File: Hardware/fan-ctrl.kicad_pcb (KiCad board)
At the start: 2 copper layers, 53 parts, among them CN1 DB127S-3.5-4P-GN, Q1 AO3401A, Q2 AO3400A, U1 STM32G070RBT6, U2 826629-3, U3 826629-3, U4 MP2359DT-LF-Z, U5 XDJK-0051-025, U6 AMS1117-3.3, Y1 Crystal_GND24

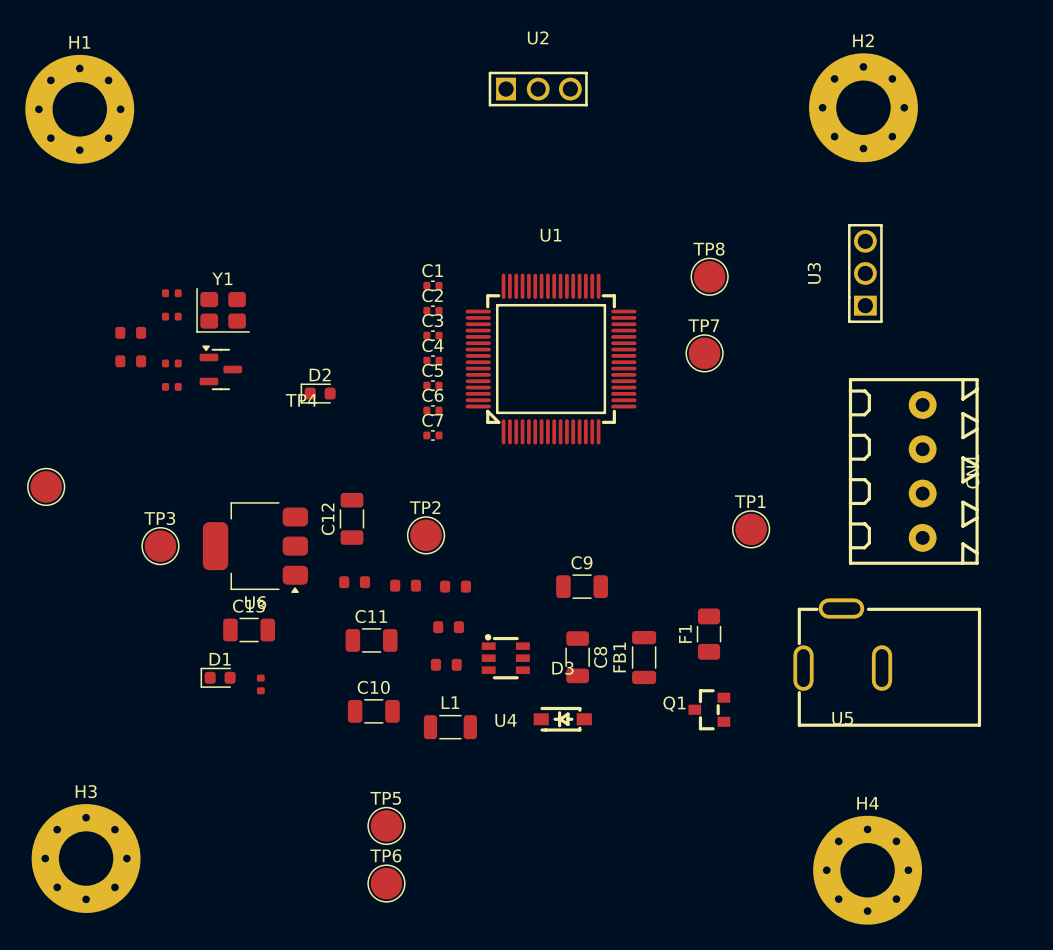
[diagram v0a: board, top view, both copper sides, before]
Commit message: Component placement, board edge cuts, adjust some footprints, testpoints, silkscreen for connectors and testpoints, next: review footprints JLCPCB before routing
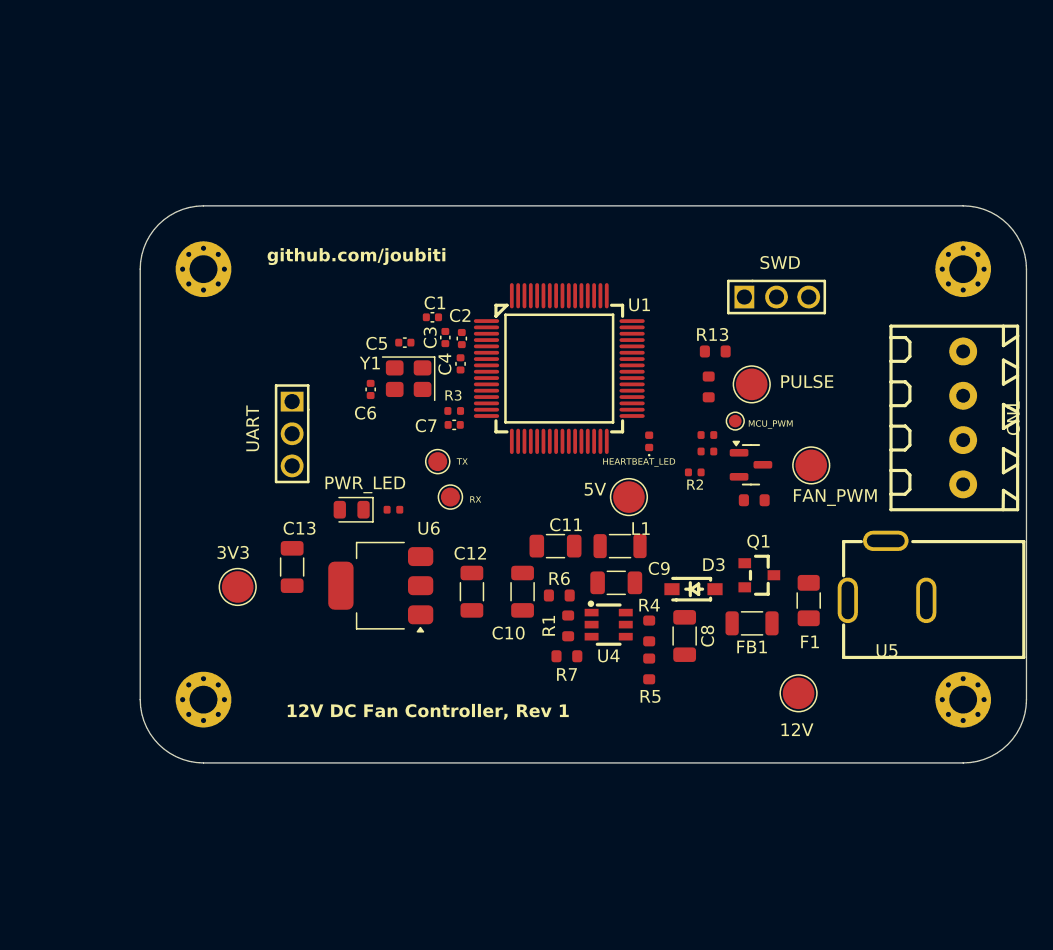
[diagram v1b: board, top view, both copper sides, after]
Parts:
- added R13: 10k, PCM_JLCPCB:R_0603, F.Cu at (163.4, 69.5)
- D1: footprint LED_SMD:LED_0603_1608Metric -> LED_SMD:LED_0805_2012Metric
- D2: footprint LED_SMD:LED_0603_1608Metric -> LED_SMD:LED_0402_1005Metric
- H1, H2, H3, H4: footprint MountingHole:MountingHole_4.3mm_M4_Pad_Via -> MountingHole:MountingHole_2.2mm_M2_Pad_Via
- TP4: footprint TestPoint:TestPoint_Pad_D2.5mm -> TestPoint:TestPoint_Pad_D1.0mm
- TP7, TP8: footprint TestPoint:TestPoint_Pad_D2.5mm -> TestPoint:TestPoint_Pad_D1.5mm
- moved TP4 54.7 mm to (165.0, 75.0)
- moved R10 50.5 mm to (166.5, 81.2)
- moved TP6 48.9 mm to (166.3, 72.1)
- moved U3 47.0 mm to (130.0, 76.0), turned to -90 degrees
- moved R9 45.8 mm to (162.9, 72.3), turned to -90 degrees
- moved TP5 44.0 mm to (171.0, 78.5)
- moved R2 43.7 mm to (161.8, 79.0)
- moved R11 42.7 mm to (162.8, 76.1)
- moved R12 42.6 mm to (162.8, 77.4)
- moved Q2 42.5 mm to (166.2, 78.5)
- moved TP8 26.9 mm to (142.5, 81.0)
- moved D2 26.3 mm to (158.2, 76.6), turned to 90 degrees
- moved U2 25.0 mm to (168.3, 65.2)
- moved R3 23.5 mm to (142.8, 74.2)
- moved TP7 22.7 mm to (141.5, 78.2)
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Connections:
- CN1 pad 1: +12V -> FAN_PULSE_IN
- CN1 pad 2: VSS -> FAN_PWM_INPUT
- CN1 pad 3: FAN_PULSE_IN -> VSS
- CN1 pad 4: FAN_PWM_INPUT -> +12V
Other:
- board outline added: 70 x 44 mm
- board text added: "12V"
- board text added: "12V DC Fan Controller, Rev 1"
- board text added: "3V3"
- board text added: "5V"
- board text added: "FAN_PWM"
- board text added: "HEARTBEAT_LED"
- board text added: "MCU_PWM"
- board text added: "PULSE"
- board text added: "PWR_LED"
- board text added: "RX"
- board text added: "SWD"
- board text added: "TX"
- board text added: "UART"
- board text added: "github.com/joubiti"

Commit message: Adjust board dimensions and edge cuts
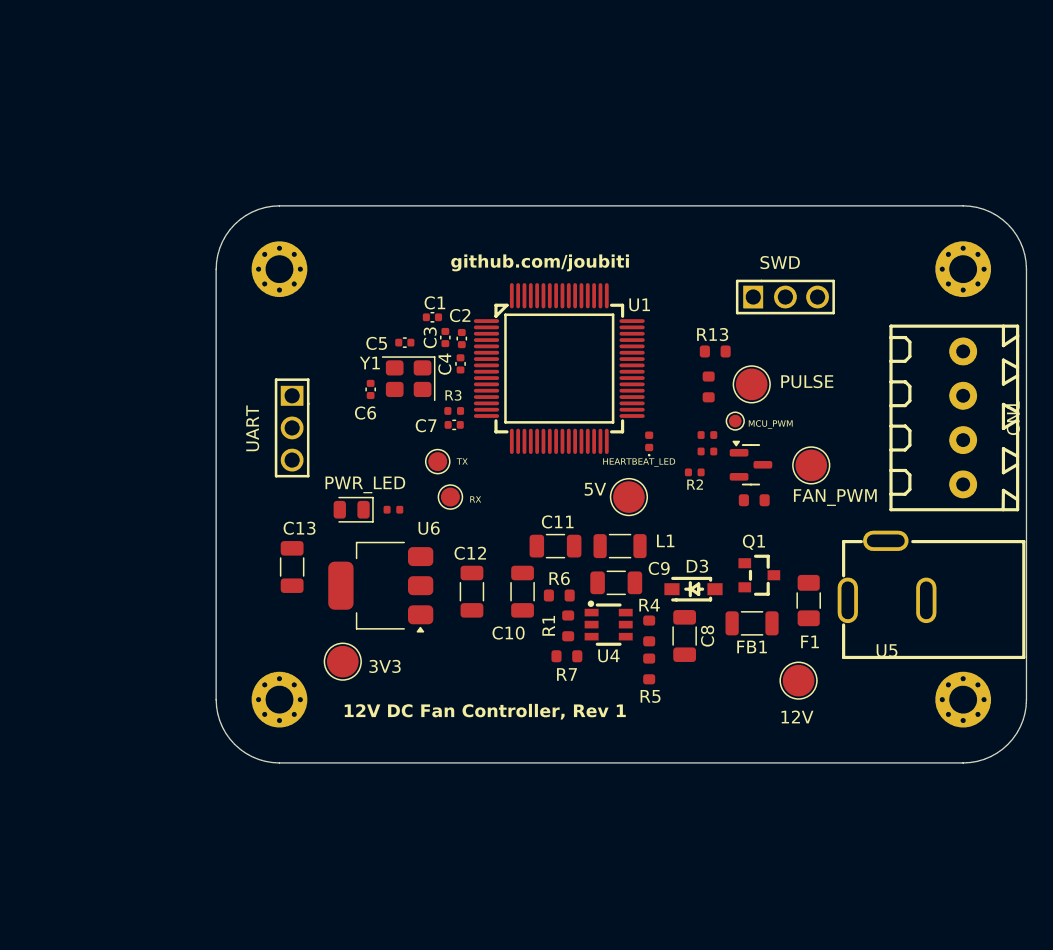
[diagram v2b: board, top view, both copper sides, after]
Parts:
- moved TP3 10.2 mm to (134.0, 94.0)
- moved H1 6.00 mm to (129.0, 63.0)
- moved H3 6.00 mm to (129.0, 97.0)
- moved TP1 1.00 mm to (170.0, 95.5)
- moved U2 0.70 mm to (169.0, 65.2)
- moved U3 0.46 mm to (130.0, 75.5)
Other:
- board size 70 x 44 mm -> 64 x 44 mm
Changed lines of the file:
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@@
 	(footprint "TestPoint:TestPoint_Pad_D2.5mm"
 		(layer "F.Cu")
-		(at 170 96.5)
+		(at 170 95.5)
 		(descr "SMD pad as test Point, diameter 2.5mm")
 		(tags "test point SMD pad")
@@
 		(at 166.9 87.175 180)
 		(property "Reference" "Q1"
-			(at 0.05 2.65 0)
+			(at 0.4 2.65 0)
 			(layer "F.SilkS")
 			(effects
@@
 	(footprint "MountingHole:MountingHole_2.2mm_M2_Pad_Via"
 		(layer "F.Cu")
-		(at 123 97)
+		(at 129 97)
 		(descr "Mounting Hole 2.2mm, M2, generated by kicad-footprint-generator mountinghole.py")
 		(tags "mountinghole M2")
@@
 		(at 161.7 88.275)
 		(property "Reference" "D3"
-			(at 1.6 -1.9 0)
+			(at 0.3 -1.775 0)
 			(layer "F.SilkS")
 			(effects
@@
 	(footprint "TestPoint:TestPoint_Pad_D2.5mm"
 		(layer "F.Cu")
-		(at 125.7 88.1)
+		(at 134 94)
 		(descr "SMD pad as test Point, diameter 2.5mm")
 		(tags "test point SMD pad")
@@
 	(footprint "MountingHole:MountingHole_2.2mm_M2_Pad_Via"
 		(layer "F.Cu")
-		(at 123 63)
+		(at 129 63)
 		(descr "Mounting Hole 2.2mm, M2, generated by kicad-footprint-generator mountinghole.py")
 		(tags "mountinghole M2")
@@
 		(tags "inductor")
 		(property "Reference" "L1"
-			(at -1.65 1.35 0)
+			(at -3.6 0.375 0)
 			(layer "F.SilkS")
 			(effects
@@
 	(footprint "easyeda2kicad:HDR-TH_3P-P2.54-V-M-1"
 		(layer "F.Cu")
-		(at 168.26 65.2)
+		(at 168.96 65.2)
 		(property "Reference" "U2"
 			(at 0 -2.5 0)
@@
 		(tags "capacitor")
 		(property "Reference" "C11"
-			(at -0.85 1.65 0)
+			(at -0.2 1.875 0)
 			(layer "F.SilkS")
 			(effects
@@
 	(footprint "easyeda2kicad:HDR-TH_3P-P2.54-V-M-1"
 		(layer "F.Cu")
-		(at 130 76 -90)
+		(at 130 75.54 -90)
 		(property "Reference" "U3"
 			(at -0.14 -2.6 90)
@@
 		)
 	)
-	(gr_arc
-		(start 183 58)
-		(mid 186.535534 59.464466)
-		(end 188 63)
+	(gr_line
+		(start 124 63)
+		(end 124 97)
 		(stroke
 			(width 0.05)
@@
 	)
 	(gr_arc
-		(start 118 63)
-		(mid 119.464466 59.464466)
-		(end 123 58)
+		(start 183 58)
+		(mid 186.535534 59.464466)
+		(end 188 63)
 		(stroke
 			(width 0.05)
@@
 		(layer "Edge.Cuts")
 	)
-	(gr_line
-		(start 123 58)
-		(end 183 58)
+	(gr_arc
+		(start 188 97)
+		(mid 186.535534 100.535534)
+		(end 183 102)
 		(stroke
 			(width 0.05)
@@
 	)
 	(gr_line
-		(start 123 102)
+		(start 129 102)
 		(end 183 102)
 		(stroke
@@
 	)
 	(gr_arc
-		(start 188 97)
-		(mid 186.535534 100.535534)
-		(end 183 102)
+		(start 124 63)
+		(mid 125.464466 59.464466)
+		(end 129 58)
 		(stroke
 			(width 0.05)
@@
 	)
 	(gr_arc
-		(start 123 102)
-		(mid 119.464466 100.535534)
-		(end 118 97)
+		(start 129 102)
+		(mid 125.464466 100.535534)
+		(end 124 97)
 		(stroke
 			(width 0.05)
@@
 	)
 	(gr_line
-		(start 118 97)
-		(end 118 63)
+		(start 129 58)
+		(end 183 58)
 		(stroke
 			(width 0.05)
@@
 	)
 	(gr_text "3V3"
-		(at 124 86 0)
+		(at 136 95 0)
 		(layer "F.SilkS")
 		(effects
@@
 	)
 	(gr_text "github.com/joubiti"
-		(at 128 62.5 0)
+		(at 142.5 63 0)
 		(layer "F.SilkS")
 		(effects
@@
 	)
 	(gr_text "12V DC Fan Controller, Rev 1"
-		(at 129.5 98.5 0)
+		(at 134 98.5 0)
 		(layer "F.SilkS")
 		(effects
@@
 	)
 	(gr_text "12V"
-		(at 168.5 100 0)
+		(at 168.5 99 0)
 		(layer "F.SilkS")
 		(effects

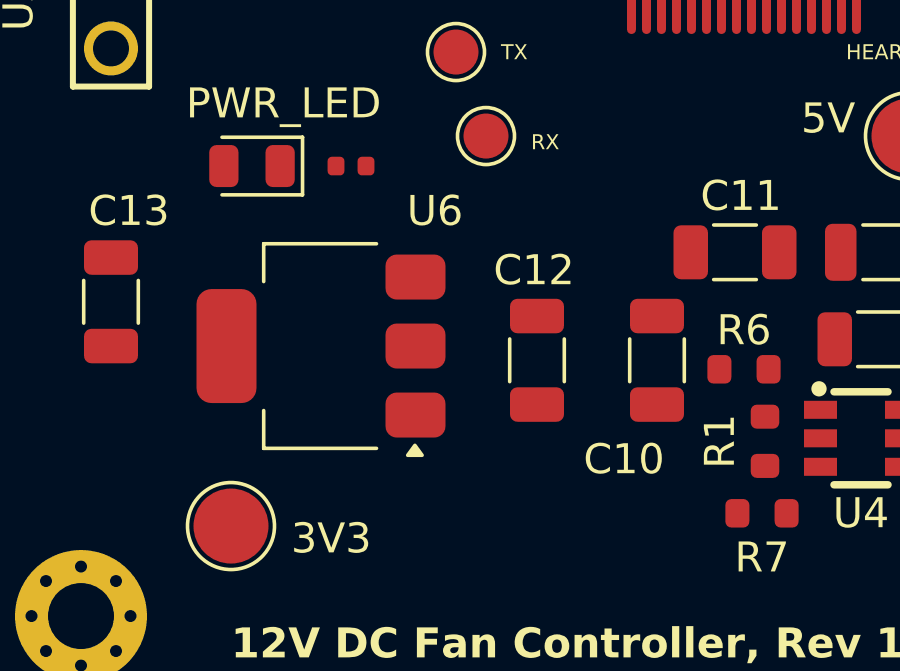
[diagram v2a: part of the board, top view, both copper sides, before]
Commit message: Update buck converter circuit, standard R values for close 5V output, double-checked footprints available in JLCPCB
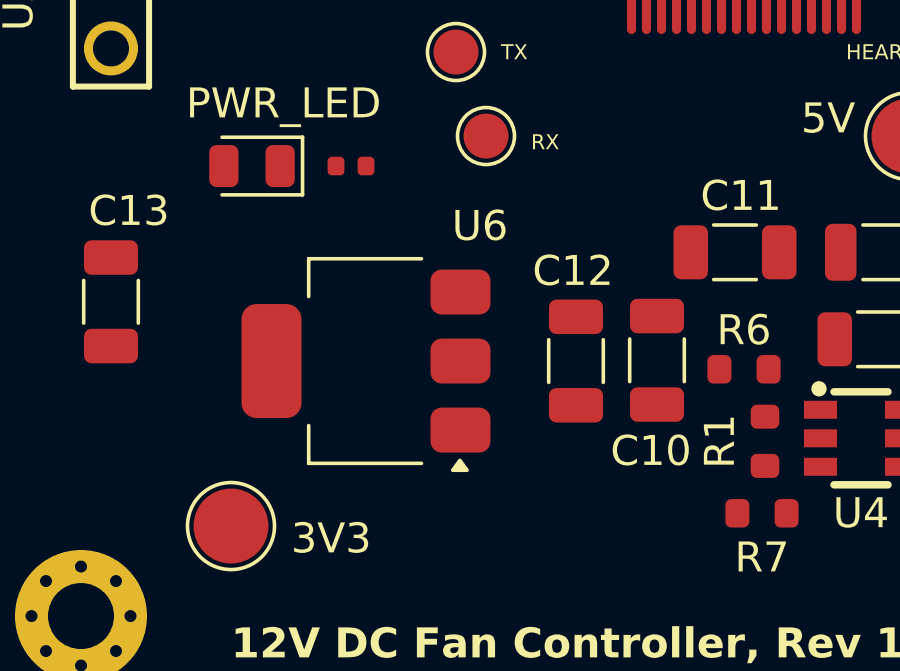
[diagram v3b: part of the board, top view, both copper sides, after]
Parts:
- L1: value 10u -> 4.7u
- R1: value 3k -> 49k9
- R7: value 10k -> 9k1
- moved U6 1.58 mm to (138.5, 88.5)
- moved C12 1.30 mm to (145.5, 88.5)
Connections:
- R1 pad 1: Net-(R1-Pad1) -> +5V
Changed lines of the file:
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@@
 	(footprint "Capacitor_SMD:C_1206_3216Metric"
 		(layer "F.Cu")
-		(at 144.2 88.475 90)
+		(at 145.5 88.5 90)
 		(descr "Capacitor SMD 1206 (3216 Metric), square (rectangular) end terminal, IPC-7351 nominal, (Body size source: IPC-SM-782 page 76, https://www.pcb-3d.com/wordpress/wp-content/uploads/ipc-sm-782a_amendment_1_and_2.pdf), generated with kicad-footprint-generator")
 		(tags "capacitor")
@@
 			)
 		)
-		(property "Value" "10k"
+		(property "Value" "9k1"
 			(at 0 1.43 0)
 			(layer "F.Fab")
@@
 		(tags "capacitor")
 		(property "Reference" "C10"
-			(at -3.3 -1.1 180)
+			(at -3.025 -0.2 180)
 			(layer "F.SilkS")
 			(effects
@@
 			)
 		)
-		(property "Value" "10u"
+		(property "Value" "4.7u"
 			(at 0 1.9 0)
 			(layer "F.Fab")
@@
 			)
 		)
-		(property "Value" "3k"
+		(property "Value" "49k9"
 			(at 0 1.43 90)
 			(layer "F.Fab")
@@
 			(layers "F.Cu" "F.Mask" "F.Paste")
 			(roundrect_rratio 0.25)
-			(net 19 "Net-(R1-Pad1)")
+			(net 8 "+5V")
 			(pintype "passive")
 		)
@@
 	(footprint "Package_TO_SOT_SMD:SOT-223-3_TabPin2"
 		(layer "F.Cu")
-		(at 137 88 180)
+		(at 138.5 88.5 180)
 		(descr "module CMS SOT223 4 pins")
 		(tags "CMS SOT")

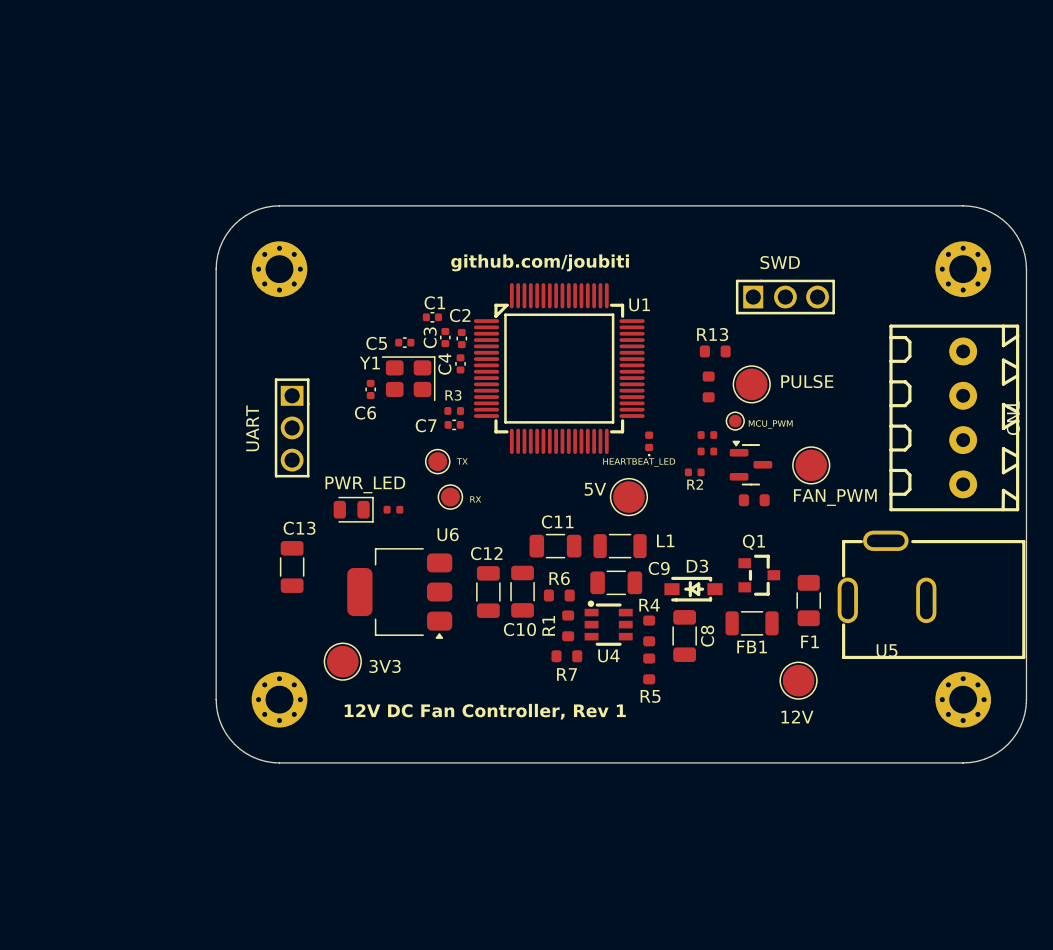
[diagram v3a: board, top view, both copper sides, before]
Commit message: Update schematics (polyfuse value, capacitor values in linear regulatorcircuit, use different HW timer enabled pin for the fan pulse input
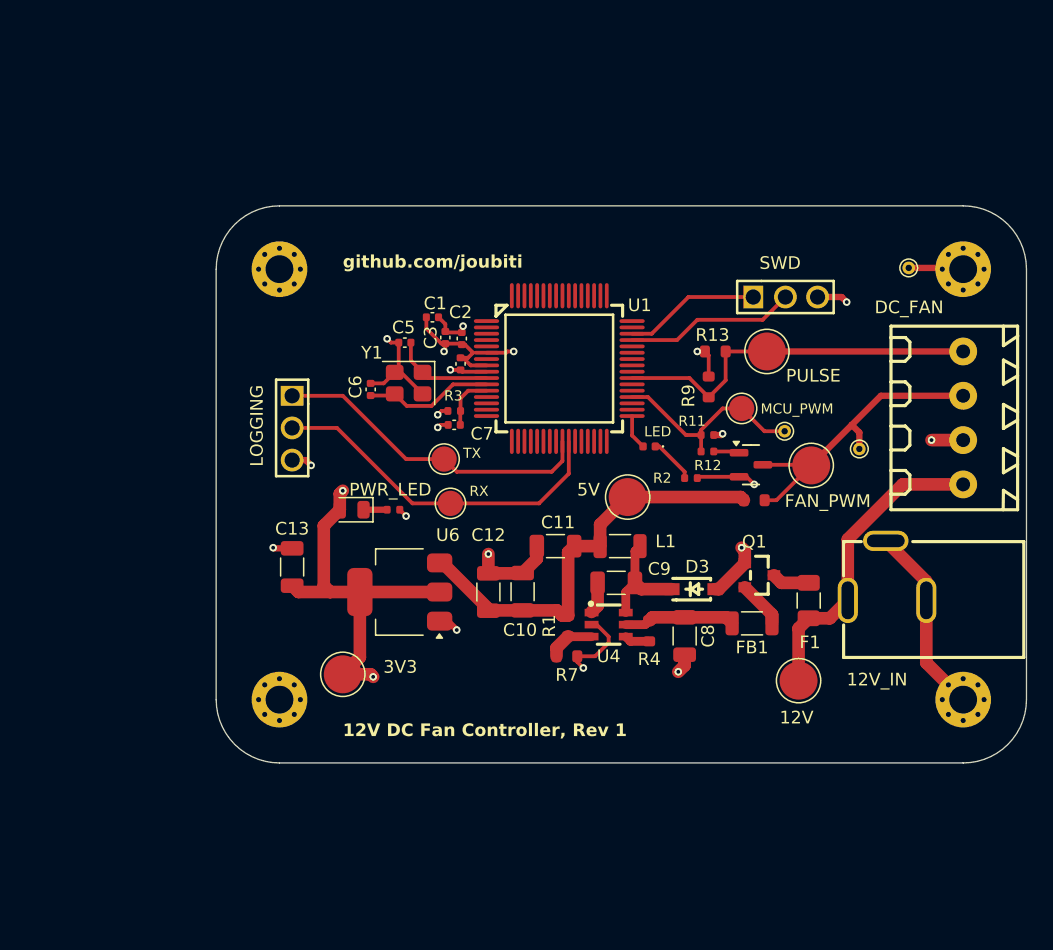
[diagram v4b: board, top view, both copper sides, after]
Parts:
- removed R5: 40k, PCM_JLCPCB:R_0603
- removed R6: 47k, PCM_JLCPCB:R_0603
- added TP10: TestPoint, TestPoint:TestPoint_THTPad_D1.0mm_Drill0.5mm, F.Cu at (174.8, 77.2)
- added TP11: TestPoint, TestPoint:TestPoint_THTPad_D1.0mm_Drill0.5mm, F.Cu at (178.7, 62.9)
- added TP9: TestPoint, TestPoint:TestPoint_THTPad_D1.0mm_Drill0.5mm, F.Cu at (168.9, 75.8)
- R4: value 120k -> 100k
- TP1, TP2, TP3, TP5, TP6: footprint TestPoint:TestPoint_Pad_D2.5mm -> TestPoint:TestPoint_Pad_D3.0mm
- TP4: footprint TestPoint:TestPoint_Pad_D1.0mm -> TestPoint:TestPoint_Pad_D2.0mm
- TP7, TP8: footprint TestPoint:TestPoint_Pad_D1.5mm -> TestPoint:TestPoint_Pad_D2.0mm
- moved TP6 2.86 mm to (167.5, 69.5)
- moved TP4 1.12 mm to (165.5, 74.0)
- moved TP3 1.00 mm to (134.0, 95.0)
- moved R2 0.54 mm to (161.5, 79.5)
- moved TP7 0.54 mm to (142.0, 78.0)
- moved TP8 0.50 mm to (142.5, 81.5)
- moved D2 0.40 mm to (158.2, 77.0), turned to 180 degrees
- moved Y1 0.35 mm to (139.2, 72.0)
- moved TP2 0.10 mm to (156.5, 81.0)
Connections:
- net VSS renamed GND
- U1 pad 39: unconnected-(U1-PC7-Pad39) -> FAN_PULSE_IN
- U1 pad 41: FAN_PULSE_IN -> unconnected-(U1-PD9-Pad41)
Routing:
- net GND: track 0.00 -> 70.4 mm, vias 0 -> 16
- net VDD: track 0.00 -> 45.3 mm, vias 0 -> 6
- net +5V: track 0.00 -> 33.8 mm
- net FAN_PULSE_IN: track 0.00 -> 29.6 mm
- net UART1_RX: track 0.00 -> 27.8 mm
- net UART1_TX: track 0.00 -> 25.7 mm
- net FAN_PWM_INPUT: track 0.00 -> 25.1 mm
- net +12V: track 0.00 -> 24.7 mm
- net MCU_PWM_OUTPUT: track 0.00 -> 16.4 mm
- net SWDIO: track 0.00 -> 13.5 mm
- net SWCLK: track 0.00 -> 10.8 mm
- net OSC_OUT: track 0.00 -> 10.3 mm
- net BUCK_SW: track 0.00 -> 8.85 mm
- net BUCK_IN: track 0.00 -> 8.83 mm
- net OSC_IN: track 0.00 -> 7.97 mm
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- added copper zone on In1.Cu, net GND
- added copper zone on In2.Cu, net VDD
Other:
- copper layers 2 -> 4
- board text added: "12V_IN"
- board text added: "DC_FAN"
- board text added: "LED"
- board text added: "LOGGING"
- board text removed: "HEARTBEAT_LED"
- board text removed: "UART"
